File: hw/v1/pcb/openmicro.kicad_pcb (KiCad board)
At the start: 4 copper layers, 95 x 95 mm, 88 parts, among them J1 ThumbPointer, J2 Debug_2x3, J3 USB_C_Receptacle_2_0, SW1 RotaryEC11, SW10 KeySwitch, SW11 KeySwitch, SW12 KeySwitch, SW13 KeySwitch, SW14 KeySwitch, SW15 KeySwitch, SW3 KeySwitch, SW4 KeySwitch, SW5 KeySwitch, SW6 KeySwitch, SW7 KeySwitch, SW8 KeySwitch, SW9 KeySwitch, U1 USBLC6, U2 AP2112K_3V3, U3 STM32F072CBT6, Y1 Crystal8MHz

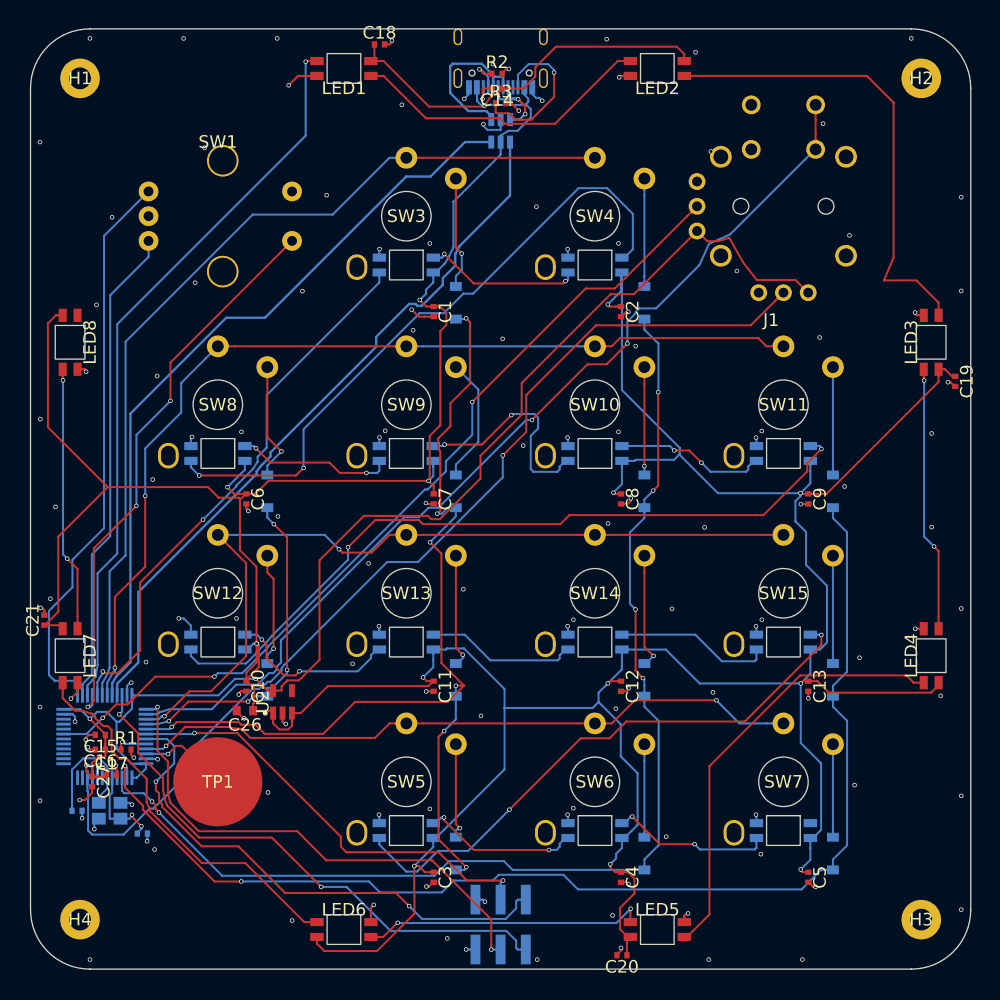
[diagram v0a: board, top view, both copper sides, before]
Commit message: hw/v1: re-routed board and regenerated production package
The board was re-routed against the corrected SK6812 and SWD-socket lands —
the previous routing was tied to the mirrored LED footprint and could not be
salvaged. Zones were refilled in KiCad and the result promoted to pcb/ as the
release board.

DRC: 0 unconnected items, 0 schematic-parity errors. The remaining flags are
the accepted classes, now stated with this routing's real numbers in
fab/README.md — clearance and track-width flags from routing to a 0.15 mm
constraint class against the board's conservative 8 mil rule, the
reverse-mount LED pads that border their own cutout by construction, the
edge-mount USB-C shield tabs, and cosmetic silkscreen warnings.

The package is regenerated whole: 11 Gerbers, PTH/NPTH Excellon drills, the
upload zip, the assembly BOM, and the pick-and-place and all-footprint
position files. Designators agree exactly across netlist, board, BOM and both
position files. fw_flash/ carries the SWD flashing instructions and pin map for
the assembly house, and obj/ keeps the autorouter candidate this board came
from.

Co-Authored-By: Claude Fable 5 <noreply@anthropic.com>
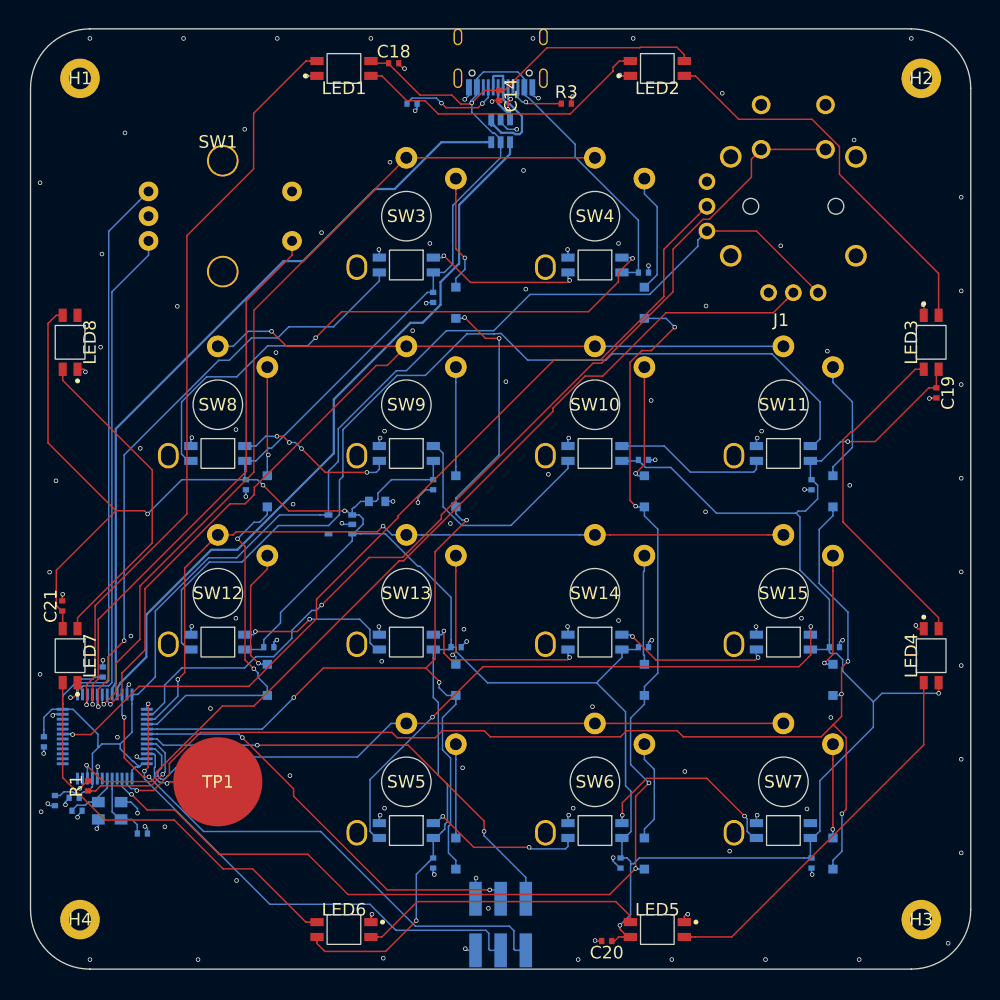
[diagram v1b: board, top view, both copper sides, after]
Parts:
- C1, C10, C11, C12, C13, C15, C16, C17, C2, C26, C27, C3, C4, C5, C6, C7, C8, C9, R2: moved to B.Cu
- D1, D10, D11, D12, D13, D2, D3, D4, D5, D6, D7, D8, D9: footprint openmicro-FP_D_SOD_123 -> diode-FP_D_SOD_123
- J2: value Debug_2x3 -> Socket_2x3; footprint openmicro-FP_Socket_2x3_254_SMD -> connectors-headers-smd_254-FP_Socket_2x3_254_SMD
- J3: footprint std-FP_USB_C_Receptacle_HRO_TYPE_C_31_M_12 -> usb-connectors-type_c-FP_USB_C_Receptacle_HRO_TYPE_C_31_M_12
- LED1, LED17, LED18, LED19, LED2, LED20, LED21, LED22, LED23, LED24, LED25, LED26, LED27, LED28, LED29, LED3, LED4, LED5, LED6, LED7, LED8: footprint openmicro-FP_LED_SK6812MINI_E -> led-FP_LED_SK6812MINI_E
- U1: footprint openmicro-FP_SOT_23_6 -> esd-FP_SOT_23_6
- U2: footprint std-SOT5P95X290X160N -> ldo-SOT5P95X290X160N; moved to B.Cu
- U3: footprint openmicro-QFP50P900X900X160_48N -> st_stm32-f0-stm32f072cb-QFP50P900X900X160_48N
- Y1: footprint openmicro-FP_Crystal_3225 -> osc-FP_Crystal_3225
- moved C26 25.0 mm to (-12.5, 0.24), turned to 0 degrees
- moved U2 18.9 mm to (-16.2, 2.56), turned to 180 degrees
- moved R2 9.10 mm to (-8.95, -39.9)
- moved C16 7.84 mm to (-40.2, 17.5), turned to 90 degrees
- moved R3 6.63 mm to (6.64, -39.9)
- moved C15 5.75 mm to (-46.1, 24.5), turned to -90 degrees
- moved R1 5.32 mm to (-41.7, 29.0), turned to 90 degrees
- moved C13 4.74 mm to (33.7, 15.0), turned to 0 degrees
- moved C11 4.55 mm to (-4.50, 15.0), turned to 0 degrees
- moved C10 4.55 mm to (-23.4, 15.0), turned to 0 degrees
- moved C12 4.55 mm to (14.4, 15.0), turned to 0 degrees
- moved C2 4.55 mm to (14.4, -22.9), turned to 0 degrees
- moved C8 4.55 mm to (14.4, -3.95), turned to 0 degrees
- moved C17 4.39 mm to (-43.1, 30.2), turned to 180 degrees
- moved C27 4.21 mm to (-45.0, 30.5)
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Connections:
- J1 pad SB: JOY_SW -> GND
- J1 pad SC: GND -> JOY_SW
- LED1 pad 1: VBUS -> GND
- LED1 pad 2: UG_D1 -> UG_D0
- LED1 pad 3: GND -> VBUS
- LED1 pad 4: UG_D0 -> UG_D1
- LED17 pad 1: VBUS -> GND
- LED17 pad 2: LED_D1 -> LED_D0
- LED17 pad 3: GND -> VBUS
- LED17 pad 4: LED_D0 -> LED_D1
- LED18 pad 1: VBUS -> GND
- LED18 pad 2: LED_D2 -> LED_D1
- LED18 pad 3: GND -> VBUS
- LED18 pad 4: LED_D1 -> LED_D2
- LED19 pad 1: VBUS -> GND
- LED19 pad 2: LED_D11 -> LED_D10
- LED19 pad 3: GND -> VBUS
- LED19 pad 4: LED_D10 -> LED_D11
- LED2 pad 1: VBUS -> GND
- LED2 pad 2: UG_D2 -> UG_D1
- LED2 pad 3: GND -> VBUS
- LED2 pad 4: UG_D1 -> UG_D2
- LED20 pad 1: VBUS -> GND
- LED20 pad 2: LED_D12 -> LED_D11
- LED20 pad 3: GND -> VBUS
- LED20 pad 4: LED_D11 -> LED_D12
- LED21 pad 1: VBUS -> GND
- LED21 pad 2: (no net) -> LED_D12
- LED21 pad 3: GND -> VBUS
- LED21 pad 4: LED_D12 -> (no net)
- LED22 pad 1: VBUS -> GND
- LED22 pad 2: LED_D3 -> LED_D2
- LED22 pad 3: GND -> VBUS
- LED22 pad 4: LED_D2 -> LED_D3
- LED23 pad 1: VBUS -> GND
- LED23 pad 2: LED_D4 -> LED_D3
- LED23 pad 3: GND -> VBUS
- LED23 pad 4: LED_D3 -> LED_D4
- LED24 pad 1: VBUS -> GND
- LED24 pad 2: LED_D5 -> LED_D4
- LED24 pad 3: GND -> VBUS
- LED24 pad 4: LED_D4 -> LED_D5
- LED25 pad 1: VBUS -> GND
- LED25 pad 2: LED_D6 -> LED_D5
- LED25 pad 3: GND -> VBUS
- LED25 pad 4: LED_D5 -> LED_D6
- LED26 pad 1: VBUS -> GND
- LED26 pad 2: LED_D7 -> LED_D6
- LED26 pad 3: GND -> VBUS
- LED26 pad 4: LED_D6 -> LED_D7
- LED27 pad 1: VBUS -> GND
- LED27 pad 2: LED_D8 -> LED_D7
- LED27 pad 3: GND -> VBUS
- LED27 pad 4: LED_D7 -> LED_D8
- LED28 pad 1: VBUS -> GND
- LED28 pad 2: LED_D9 -> LED_D8
- LED28 pad 3: GND -> VBUS
- LED28 pad 4: LED_D8 -> LED_D9
- LED29 pad 1: VBUS -> GND
- LED29 pad 2: LED_D10 -> LED_D9
- LED29 pad 3: GND -> VBUS
- LED29 pad 4: LED_D9 -> LED_D10
- LED3 pad 1: VBUS -> GND
- LED3 pad 2: UG_D3 -> UG_D2
- LED3 pad 3: GND -> VBUS
- LED3 pad 4: UG_D2 -> UG_D3
- LED4 pad 1: VBUS -> GND
- LED4 pad 2: UG_D4 -> UG_D3
- LED4 pad 3: GND -> VBUS
- LED4 pad 4: UG_D3 -> UG_D4
- LED5 pad 1: VBUS -> GND
- LED5 pad 2: UG_D5 -> UG_D4
- LED5 pad 3: GND -> VBUS
- LED5 pad 4: UG_D4 -> UG_D5
- LED6 pad 1: VBUS -> GND
- LED6 pad 2: UG_D6 -> UG_D5
- LED6 pad 3: GND -> VBUS
- LED6 pad 4: UG_D5 -> UG_D6
- LED7 pad 1: VBUS -> GND
- LED7 pad 2: UG_D7 -> UG_D6
- LED7 pad 3: GND -> VBUS
- LED7 pad 4: UG_D6 -> UG_D7
- LED8 pad 1: VBUS -> GND
- LED8 pad 2: (no net) -> UG_D7
- LED8 pad 3: GND -> VBUS
- LED8 pad 4: UG_D7 -> (no net)
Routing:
- net VBUS: track 486.4 -> 451.0 mm, vias 14 -> 8
- net LED_D6: track 76.6 -> 95.0 mm, vias 2 -> 0
- net GND: track 74.1 -> 61.6 mm, vias 137 -> 138
- net ROW1: track 97.6 -> 109.6 mm
- net CC2: track 16.4 -> 5.67 mm
- net BOOT0: track 3.29 -> 12.7 mm
- net JOY_Y: track 103.3 -> 94.4 mm
- net UG_D2: track 48.2 -> 39.8 mm
- net UG_D3: track 26.8 -> 34.2 mm, vias 2 -> 0
- net V3V3: track 132.5 -> 139.5 mm, vias 3 -> 0
- net HSE_OUT: track 12.6 -> 5.80 mm
- net CC1: track 3.74 -> 10.3 mm, vias 1 -> 2
- net LED_D2: track 66.1 -> 59.7 mm
- net UG_D7: track 26.8 -> 33.1 mm, vias 2 -> 0
- net LED_D0: track 55.5 -> 61.7 mm
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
